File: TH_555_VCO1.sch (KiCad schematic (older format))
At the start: 73 parts, among them J601 CV1, J602 FM_lin, J603 Sync, J604 PWM, J605 Ramp, J606 Tri, J607 Sine, J608 555_Pulse, P601 Doepfer_Power_10pin, Q601 MMBT2222A, U601 TLC555, U602 TL074, U603 TL074

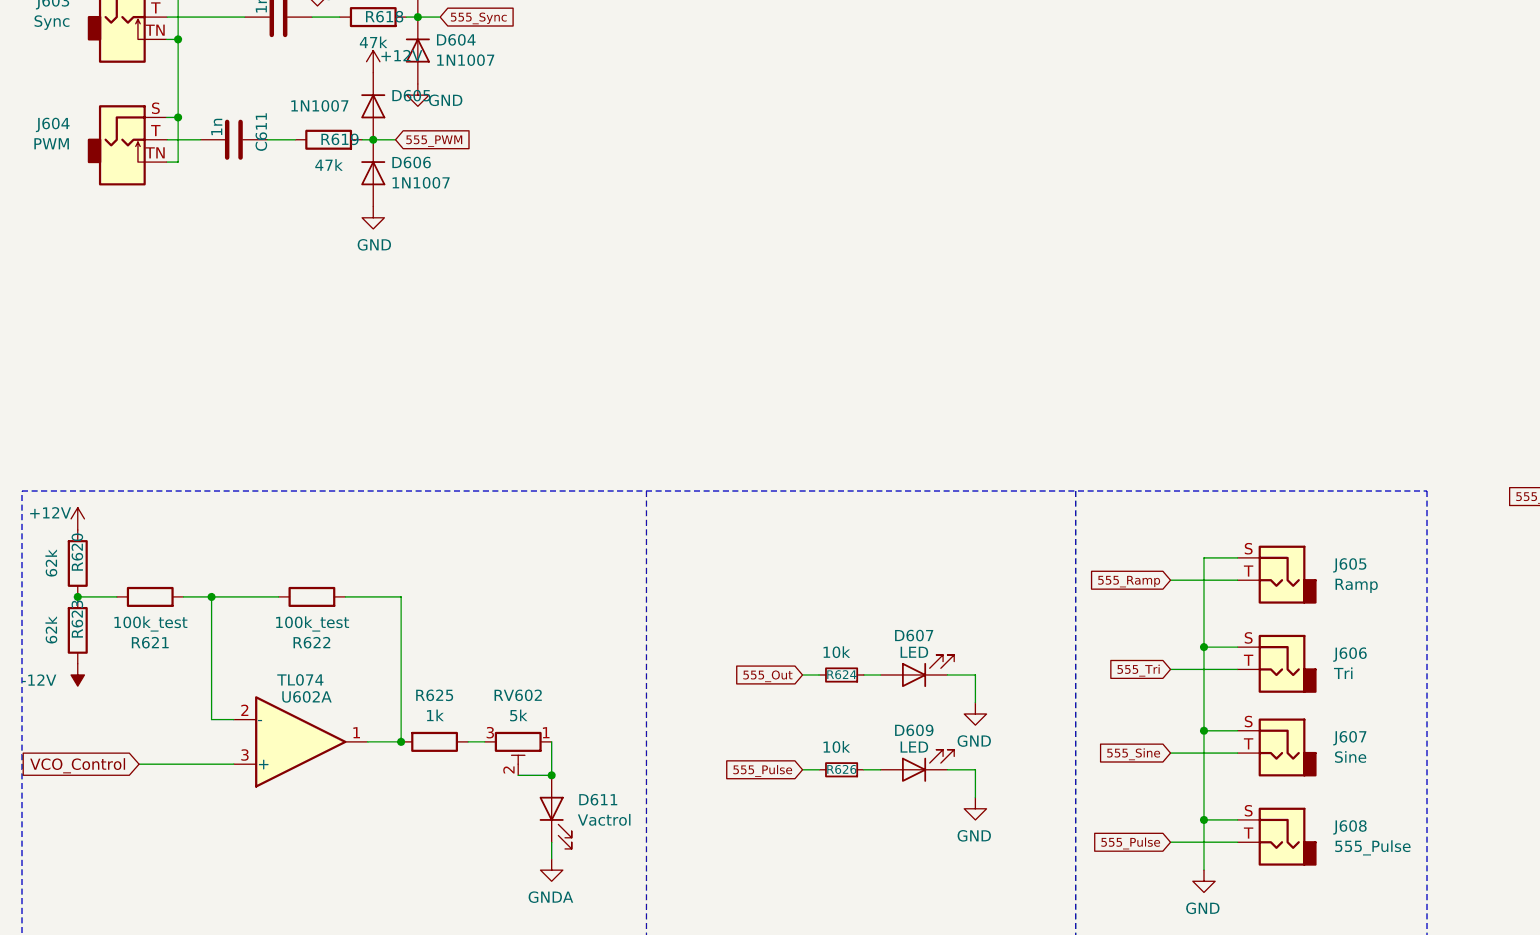
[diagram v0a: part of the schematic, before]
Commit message: Placing outputs and Pots 555
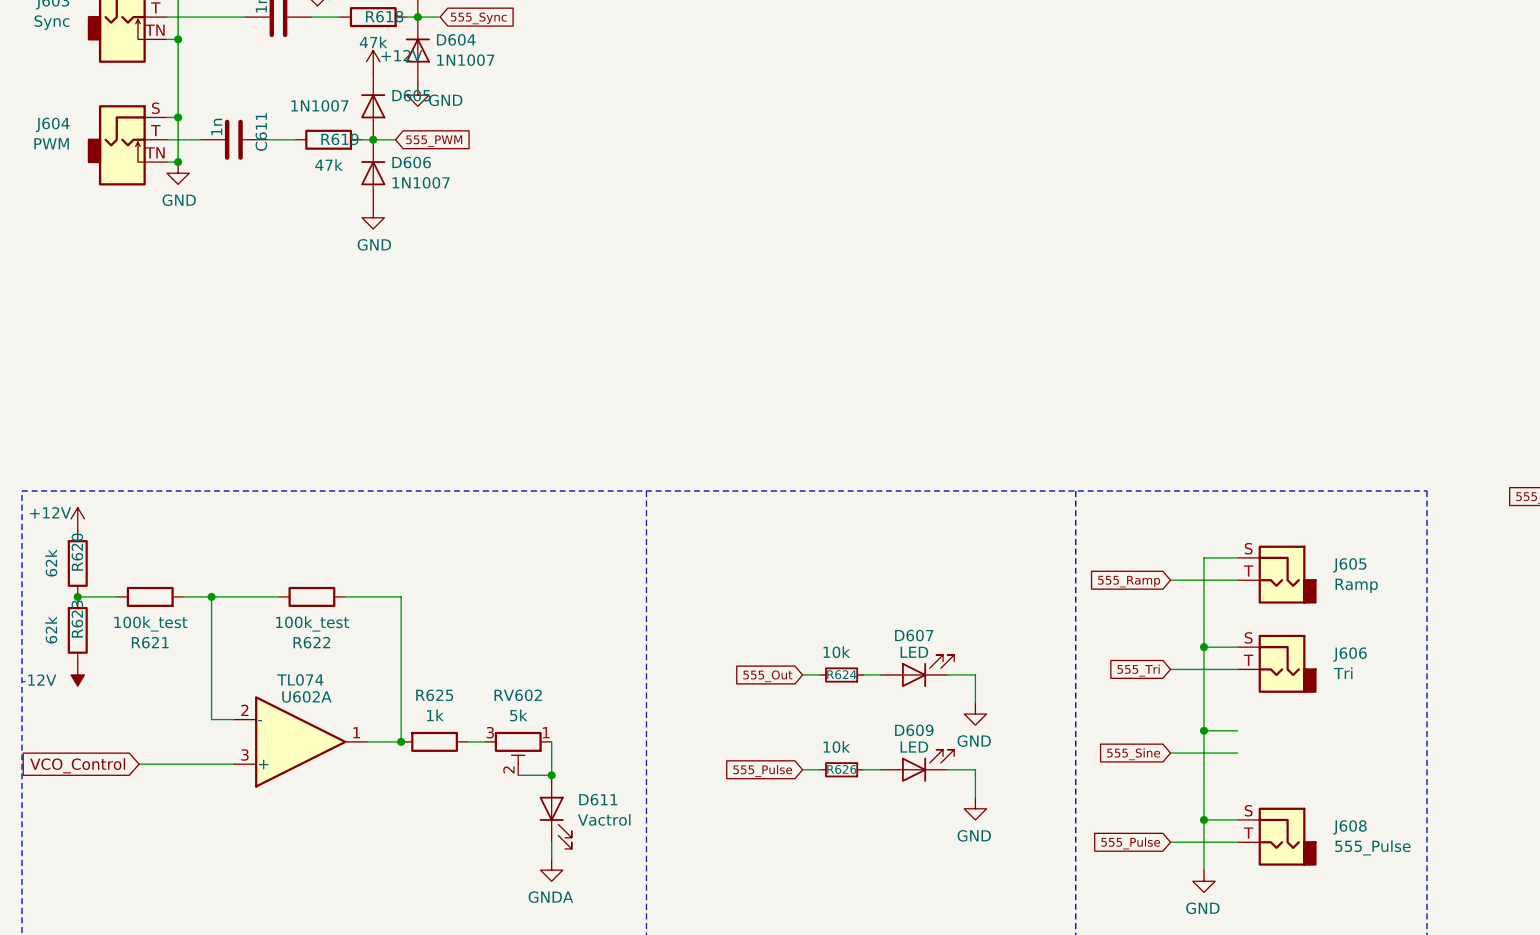
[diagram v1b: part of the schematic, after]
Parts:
- removed J607: Sine, AJ-Dropbox-Kicad:PJ301SM, symbol Connector:AudioJack2
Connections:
- net GND: now also J601.S, J601.TN, J602.S, J602.TN, J603.S, J603.TN, J604.S, J604.TN
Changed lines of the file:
@@
-$Comp
-L Connector:AudioJack2 J?
-U 1 1 5DD948CA
-P 6275 6825
-AR Path="/5DD948CA" Ref="J?"  Part="1"
-AR Path="/5D60ED9A/5DD948CA" Ref="J?"  Part="1"
-AR Path="/5CD6EBF4/5DD948CA" Ref="J?"  Part="1"
-AR Path="/5CE53731/5DD948CA" Ref="J?"  Part="1"
-AR Path="/5DD87D87/5DD948CA" Ref="J607"  Part="1"
-F 0 "J607" H 6042 6896 50  0000 R CNN
-F 1 "Sine" H 6042 6805 50  0000 R CNN
-F 2 "AJ-Dropbox-Kicad:PJ301SM" H 6275 6825 50  0001 C CNN
-F 3 "~" H 6275 6825 50  0001 C CNN
-	1    6275 6825
-	-1   0    0    -1
-$EndComp
 $Comp
 L Connector:AudioJack2 J?
@@
 	0    -1   -1   0
 $EndComp
+$Comp
+L Envelope-cache-2018-08-04-13-00-04:GND #PWR?
+U 1 1 5E3D265D
+P 1325 4175
+AR Path="/5E3D265D" Ref="#PWR?"  Part="1"
+AR Path="/5CE53731/5E3D265D" Ref="#PWR?"  Part="1"
+AR Path="/5DD87D87/5E3D265D" Ref="#PWR?"  Part="1"
+F 0 "#PWR?" H 1325 3925 50  0001 C CNN
+F 1 "GND" H 1330 4002 50  0000 C CNN
+F 2 "" H 1325 4175 50  0001 C CNN
+F 3 "" H 1325 4175 50  0001 C CNN
+	1    1325 4175
+	1    0    0    -1
+$EndComp
+Connection ~ 1325 4175
 $EndSCHEMATC

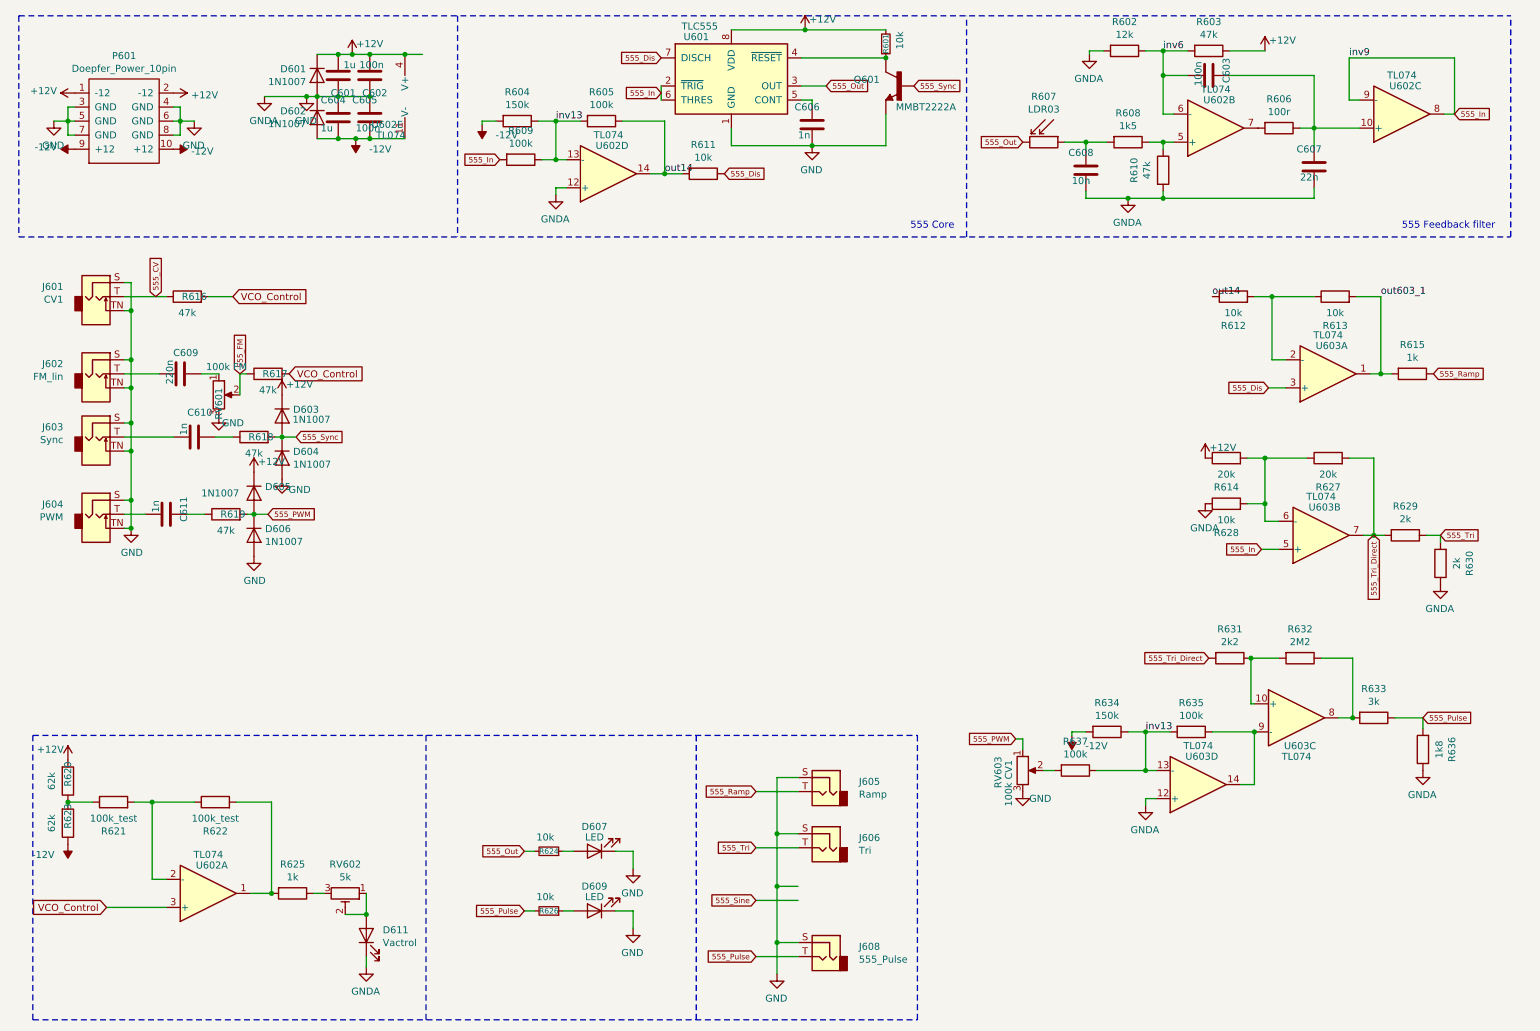
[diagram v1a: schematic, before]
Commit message: 555 Pwr to U603
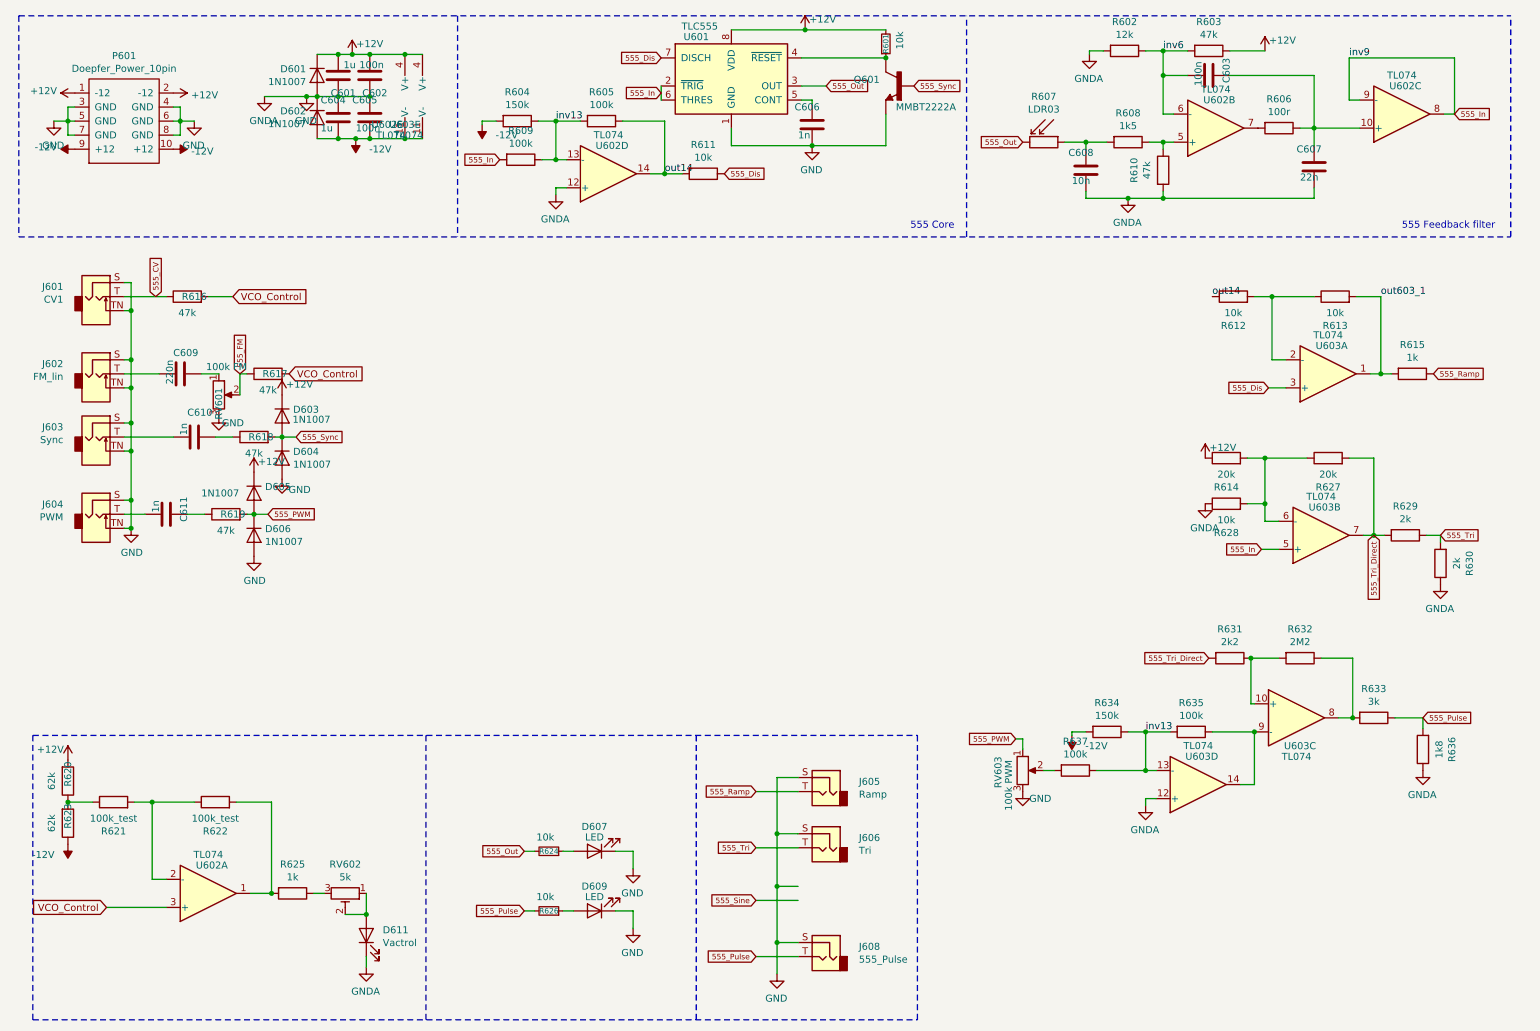
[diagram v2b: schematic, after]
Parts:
- added unit 5 of U603
- RV603: value 100k CV1 -> 100k PWM
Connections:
- net +12V: now also U603.4 (V+)
- net -12V: now also U603.11 (V-)
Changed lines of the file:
@@
 AR Path="/5DD87D87/5DD948E3" Ref="RV603"  Part="1"
 F 0 "RV603" V 7500 6000 50  0000 R CNN
-F 1 "100k CV1" V 7575 5975 50  0000 R CNN
+F 1 "100k PWM" V 7575 5975 50  0000 R CNN
 F 2 "Potentiometer_THT:Potentiometer_China_RK09_Single_Vertical_AJ" H 7675 5900 50  0001 C CNN
 F 3 "~" H 7675 5900 50  0001 C CNN
@@
 AR Path="/5E3D265D" Ref="#PWR?"  Part="1"
 AR Path="/5CE53731/5E3D265D" Ref="#PWR?"  Part="1"
-AR Path="/5DD87D87/5E3D265D" Ref="#PWR?"  Part="1"
-F 0 "#PWR?" H 1325 3925 50  0001 C CNN
+AR Path="/5DD87D87/5E3D265D" Ref="#PWR0109"  Part="1"
+F 0 "#PWR0109" H 1325 3925 50  0001 C CNN
 F 1 "GND" H 1330 4002 50  0000 C CNN
 F 2 "" H 1325 4175 50  0001 C CNN
@@
 $EndComp
 Connection ~ 1325 4175
+$Comp
+L Amplifier_Operational:TL074 U?
+U 5 1 5E3ED959
+P 3300 1100
+AR Path="/5DD87D87/5DDB8911/5E3ED959" Ref="U?"  Part="1"
+AR Path="/5DD87D87/5E3ED959" Ref="U603"  Part="5"
+F 0 "U603" H 3325 900 50  0000 C CNN
+F 1 "TL074" H 3300 824 50  0000 C CNN
+F 2 "" H 3250 1200 50  0001 C CNN
+F 3 "http://www.ti.com/lit/ds/symlink/tl071.pdf" H 3350 1300 50  0001 C CNN
+	5    3300 1100
+	-1   0    0    -1
+$EndComp
+Wire Wire Line
+	3275 1400 3400 1400
+Connection ~ 3275 1400
 $EndSCHEMATC

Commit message: Labels mixup
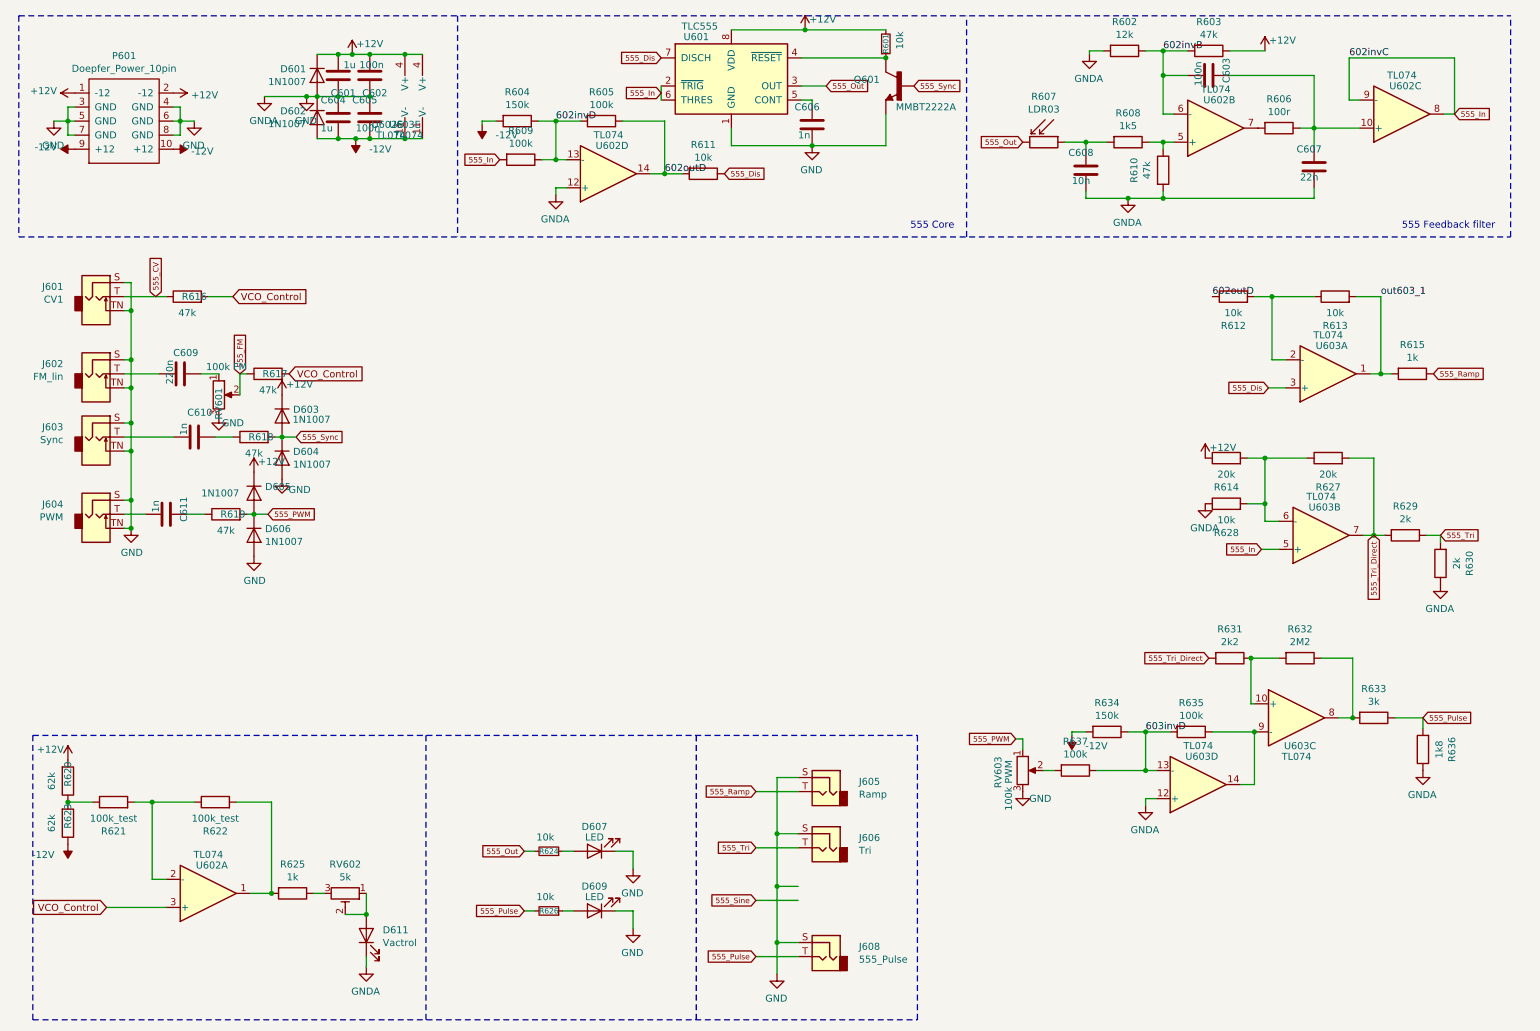
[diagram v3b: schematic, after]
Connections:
- net inv13 renamed 602invD
- net 602invD: no longer R634.1, R635.2, R637.1, U603.13 (-)
- net inv6 renamed 602invB
- net out14 renamed 602outD
- new net 603invD: R634.1, R635.2, R637.1, U603.13 (-)
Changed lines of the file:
@@
 $EndComp
 Text Label 4350 1275 0    50   ~ 0
-inv13
+602invD
 $Comp
 L Device:R R?
@@
 555_Dis
 Text Label 8675 775  0    50   ~ 0
-inv6
+602invB
 Text Label 10000 825  0    50   ~ 0
-inv9
+602invC
 $Comp
 L Device:R R?
@@
 $EndComp
 Text Label 5125 1650 0    50   ~ 0
-out14
+602outD
 Text Label 9025 2525 0    50   ~ 0
-out14
+602outD
 Text GLabel 9425 3175 0    39   Input ~ 0
 555_Dis
@@
 555_Tri_Direct
 Text Label 8550 5625 0    50   ~ 0
-inv13
+603invD
 $Comp
 L Amplifier_Operational:TL074 U?

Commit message: label sch + png
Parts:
- R634: value 150k -> OPEN
- R635: value 100k -> 120k
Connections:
- net 603invB: now reaches R614.2, R627.1, R628.2, U603.6 (-)
- net 602outD renamed 602_Out_D
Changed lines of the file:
@@
 	0    -1   -1   0
 $EndComp
-Text Label 5125 1650 0    50   ~ 0
-602outD
-Text Label 9025 2525 0    50   ~ 0
-602outD
 Text GLabel 9425 3175 0    39   Input ~ 0
 555_Dis
@@
 AR Path="/5DD87D87/5E21E990" Ref="R635"  Part="1"
 F 0 "R635" V 8668 5625 50  0000 C CNN
-F 1 "100k" V 8759 5625 50  0000 C CNN
+F 1 "120k" V 8759 5625 50  0000 C CNN
 F 2 "Resistor_SMD:R_0805_2012Metric_Pad1.15x1.40mm_HandSolder" V 8805 5625 50  0001 C CNN
 F 3 "~" H 8875 5625 50  0001 C CNN
@@
 AR Path="/5DD87D87/5E21E99D" Ref="R634"  Part="1"
 F 0 "R634" V 8068 5625 50  0000 C CNN
-F 1 "150k" V 8159 5625 50  0000 C CNN
+F 1 "OPEN" V 8159 5625 50  0000 C CNN
 F 2 "Resistor_SMD:R_0805_2012Metric_Pad1.15x1.40mm_HandSolder" V 8205 5625 50  0001 C CNN
 F 3 "~" H 8275 5625 50  0001 C CNN
@@
 AR Path="/5DD87D87/5E21E9B4" Ref="#PWR0623"  Part="1"
 F 0 "#PWR0623" H 8025 5750 50  0001 C CNN
-F 1 "-12V" H 7850 5725 50  0000 C CNN
+F 1 "-12V" H 8100 5450 50  0000 C CNN
 F 2 "" H 8025 5650 50  0001 C CNN
 F 3 "" H 8025 5650 50  0001 C CNN
@@
 	3275 1400 3400 1400
 Connection ~ 3275 1400
+Text GLabel 9025 2525 0    50   Input ~ 0
+602_Out_D
+Text GLabel 5125 1650 3    50   Input ~ 0
+602_Out_D
+Text Label 9400 3675 0    50   ~ 0
+603invB
 $EndSCHEMATC
